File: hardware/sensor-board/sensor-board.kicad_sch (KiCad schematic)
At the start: 46 parts, among them J1 QWIIC Connector, J2 QWIIC Connector, J3 3-pole terminal, J4 2-pole terminal, Q1 BSS84, U1 DS18B20, U2 DS2482S-100+, U3 PCA9501PW_118, U4 LMV601, U5 MCP96L01T-E{slash}MX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

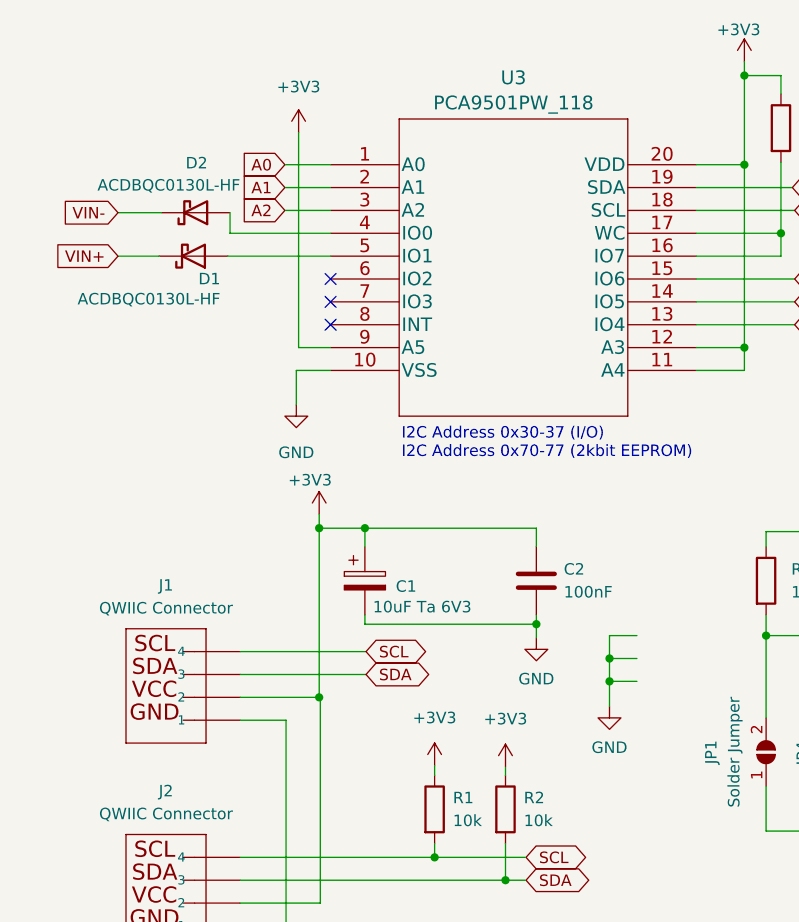
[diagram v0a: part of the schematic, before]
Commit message: Got rid of TINY diode (0402!?!?), remove USE_USB, put in PicoW
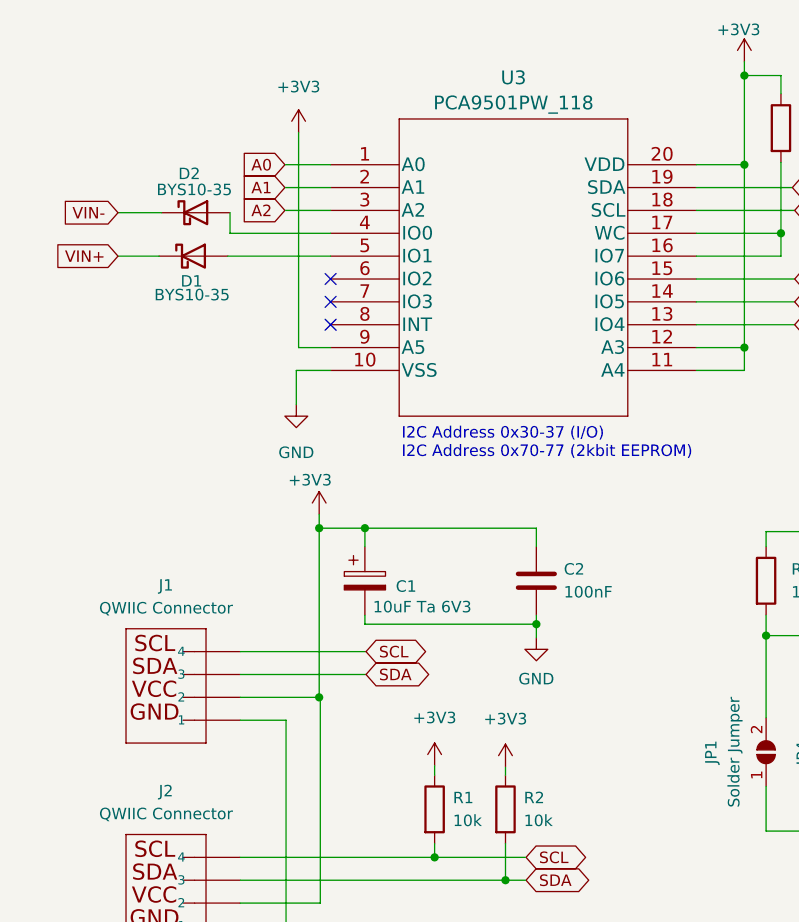
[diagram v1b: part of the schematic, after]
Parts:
- D1, D2: value ACDBQC0130L-HF -> BYS10-35; footprint Diode_SMD:D_SOD-923 -> Diode_SMD:D_SMA_Handsoldering
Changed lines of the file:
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@@
   (junction (at 128.143 128.27) (diameter 0) (color 0 0 0 0)
   )
-  (junction (at 78.232 85.598) (diameter 0) (color 0 0 0 0)
-  )
   (junction (at 97.282 35.814) (diameter 0) (color 0 0 0 0)
   )
@@
   )
   (junction (at 27.051 178.435) (diameter 0) (color 0 0 0 0)
-  )
-  (junction (at 78.232 83.058) (diameter 0) (color 0 0 0 0)
   )
   (junction (at 155.448 119.38) (diameter 0) (color 0 0 0 0)
@@
     (stroke (width 0) (type default) (color 0 0 0 0))
   )
-  (wire (pts (xy 78.232 83.058) (xy 78.232 85.598))
-    (stroke (width 0) (type default) (color 0 0 0 0))
-  )
   (wire (pts (xy 249.936 128.27) (xy 253.492 128.27))
     (stroke (width 0) (type default) (color 0 0 0 0))
@@
     (stroke (width 0) (type default) (color 0 0 0 0))
   )
-  (wire (pts (xy 78.232 85.598) (xy 78.232 88.392))
-    (stroke (width 0) (type default) (color 0 0 0 0))
-  )
   (wire (pts (xy 24.13 183.515) (xy 29.21 183.515))
     (stroke (width 0) (type default) (color 0 0 0 0))
@@
     (stroke (width 0) (type default) (color 0 0 0 0))
   )
-  (wire (pts (xy 78.232 83.058) (xy 78.232 80.518))
-    (stroke (width 0) (type default) (color 0 0 0 0))
-  )
   (wire (pts (xy 177.292 57.404) (xy 167.64 57.404))
     (stroke (width 0) (type default) (color 0 0 0 0))
@@
     (stroke (width 0) (type default) (color 0 0 0 0))
   )
-  (wire (pts (xy 81.28 85.598) (xy 78.232 85.598))
-    (stroke (width 0) (type default) (color 0 0 0 0))
-  )
   (wire (pts (xy 181.356 152.146) (xy 188.214 152.146))
     (stroke (width 0) (type default) (color 0 0 0 0))
@@
     (stroke (width 0) (type default) (color 0 0 0 0))
   )
-  (wire (pts (xy 78.232 80.518) (xy 81.28 80.518))
-    (stroke (width 0) (type default) (color 0 0 0 0))
-  )
   (wire (pts (xy 87.884 48.514) (xy 93.218 48.514))
     (stroke (width 0) (type default) (color 0 0 0 0))
@@
   )
   (wire (pts (xy 115.443 102.235) (xy 105.791 102.235))
-    (stroke (width 0) (type default) (color 0 0 0 0))
-  )
-  (wire (pts (xy 78.232 83.058) (xy 81.28 83.058))
     (stroke (width 0) (type default) (color 0 0 0 0))
   )
@@
     )
     (pin "1")
-  )
-  (symbol (lib_id "Device:D_Schottky") (at 32.004 38.354 0) (mirror x) (unit 1)
-    (in_bom yes) (on_board yes)
-    (property "Reference" "D1" (id 0) (at 35.0012 40.894 0)
-      (effects (font (size 1.27 1.27)) (justify right))
-    )
-    (property "Value" "ACDBQC0130L-HF" (id 1) (at 35.0012 43.1292 0)
-      (effects (font (size 1.27 1.27)) (justify right))
-    )
-    (property "Footprint" "Diode_SMD:D_SOD-923" (id 2) (at 32.004 38.354 0)
-      (effects (font (size 1.27 1.27)) hide)
-    )
-    (property "Datasheet" "~" (id 3) (at 32.004 38.354 0)
-      (effects (font (size 1.27 1.27)) hide)
-    )
-    (pin "1")
-    (pin "2")
   )
   (symbol (lib_id "Jumper:SolderJumper_3_Open") (at 103.886 172.339 270) (mirror x) (unit 1)
@@
     )
     (property "Datasheet" "~" (id 3) (at 156.464 66.04 0)
-      (effects (font (size 1.27 1.27)) hide)
-    )
-    (pin "1")
-    (pin "2")
-  )
-  (symbol (lib_id "Device:D_Schottky") (at 32.258 33.528 0) (mirror x) (unit 1)
-    (in_bom yes) (on_board yes)
-    (property "Reference" "D2" (id 0) (at 33.5788 28.0162 0)
-      (effects (font (size 1.27 1.27)) (justify right))
-    )
-    (property "Value" "ACDBQC0130L-HF" (id 1) (at 37.211 30.48 0)
-      (effects (font (size 1.27 1.27)) (justify right))
-    )
-    (property "Footprint" "Diode_SMD:D_SOD-923" (id 2) (at 32.258 33.528 0)
-      (effects (font (size 1.27 1.27)) hide)
-    )
-    (property "Datasheet" "~" (id 3) (at 32.258 33.528 0)
       (effects (font (size 1.27 1.27)) hide)
     )
@@
     (pin "1")
   )
+  (symbol (lib_id "Device:D_Schottky") (at 32.004 38.354 0) (unit 1)
+    (in_bom yes) (on_board yes)
+    (property "Reference" "D1" (id 0) (at 33.02 41.148 0)
+      (effects (font (size 1.27 1.27)) (justify right))
+    )
+    (property "Value" "BYS10-35" (id 1) (at 36.068 42.672 0)
+      (effects (font (size 1.27 1.27)) (justify right))
+    )
+    (property "Footprint" "Diode_SMD:D_SMA_Handsoldering" (id 2) (at 32.004 38.354 0)
+      (effects (font (size 1.27 1.27)) hide)
+    )
+    (property "Datasheet" "~" (id 3) (at 32.004 38.354 0)
+      (effects (font (size 1.27 1.27)) hide)
+    )
+    (pin "1")
+    (pin "2")
+  )
   (symbol (lib_id "Jumper:SolderJumper_2_Open") (at 115.443 93.726 90) (unit 1)
     (in_bom yes) (on_board yes)
@@
     (pin "2")
   )
+  (symbol (lib_id "Device:D_Schottky") (at 32.258 33.528 0) (unit 1)
+    (in_bom yes) (on_board yes)
+    (property "Reference" "D2" (id 0) (at 32.766 29.21 0)
+      (effects (font (size 1.27 1.27)) (justify right))
+    )
+    (property "Value" "BYS10-35" (id 1) (at 36.322 30.988 0)
+      (effects (font (size 1.27 1.27)) (justify right))
+    )
+    (property "Footprint" "Diode_SMD:D_SMA_Handsoldering" (id 2) (at 32.258 33.528 0)
+      (effects (font (size 1.27 1.27)) hide)
+    )
+    (property "Datasheet" "~" (id 3) (at 32.258 33.528 0)
+      (effects (font (size 1.27 1.27)) hide)
+    )
+    (pin "1")
+    (pin "2")
+  )
   (symbol (lib_name "GND_1") (lib_id "power:GND") (at 169.926 154.686 0) (unit 1)
     (in_bom yes) (on_board yes) (fields_autoplaced)
@@
     )
     (property "Datasheet" "" (id 3) (at 93.218 16.764 0)
-      (effects (font (size 1.27 1.27)) hide)
-    )
-    (pin "1")
-  )
-  (symbol (lib_id "power:GND") (at 78.232 88.392 0) (unit 1)
-    (in_bom yes) (on_board yes) (fields_autoplaced)
-    (property "Reference" "#PWR016" (id 0) (at 78.232 94.742 0)
-      (effects (font (size 1.27 1.27)) hide)
-    )
-    (property "Value" "GND" (id 1) (at 78.232 92.964 0))
-    (property "Footprint" "" (id 2) (at 78.232 88.392 0)
-      (effects (font (size 1.27 1.27)) hide)
-    )
-    (property "Datasheet" "" (id 3) (at 78.232 88.392 0)
       (effects (font (size 1.27 1.27)) hide)
     )
@@
       (reference "#PWR015") (unit 1) (value "GND") (footprint "")
     )
-    (path "/af7a7386-51a5-445a-ac94-e3e13c49cad7"
-      (reference "#PWR016") (unit 1) (value "GND") (footprint "")
-    )
     (path "/ad59493c-933f-43d3-ad66-dedc917b794c"
       (reference "#PWR017") (unit 1) (value "+3V3") (footprint "")
@@
       (reference "C7") (unit 1) (value "10uF Ta 6V3") (footprint "Capacitor_Tantalum_SMD:CP_EIA-3216-10_Kemet-I_Pad1.58x1.35mm_HandSolder")
     )
-    (path "/25f938d3-f303-4ec1-aea2-bab453c3efaf"
-      (reference "D1") (unit 1) (value "ACDBQC0130L-HF") (footprint "Diode_SMD:D_SOD-923")
-    )
-    (path "/41ddbbe9-c7a1-4976-9106-2036b43731a2"
-      (reference "D2") (unit 1) (value "ACDBQC0130L-HF") (footprint "Diode_SMD:D_SOD-923")
+    (path "/733d93f6-1e46-4544-9437-7f001e763c99"
+      (reference "D1") (unit 1) (value "BYS10-35") (footprint "Diode_SMD:D_SMA_Handsoldering")
+    )
+    (path "/7d3c90be-9369-4ec3-9527-906e706434c9"
+      (reference "D2") (unit 1) (value "BYS10-35") (footprint "Diode_SMD:D_SMA_Handsoldering")
     )
     (path "/9deb20ba-b373-419e-9cdf-d85d90d8e321"
